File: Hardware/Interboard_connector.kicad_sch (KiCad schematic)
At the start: 2 parts, among them J201 Chainbus in, J202 Chainbus Out

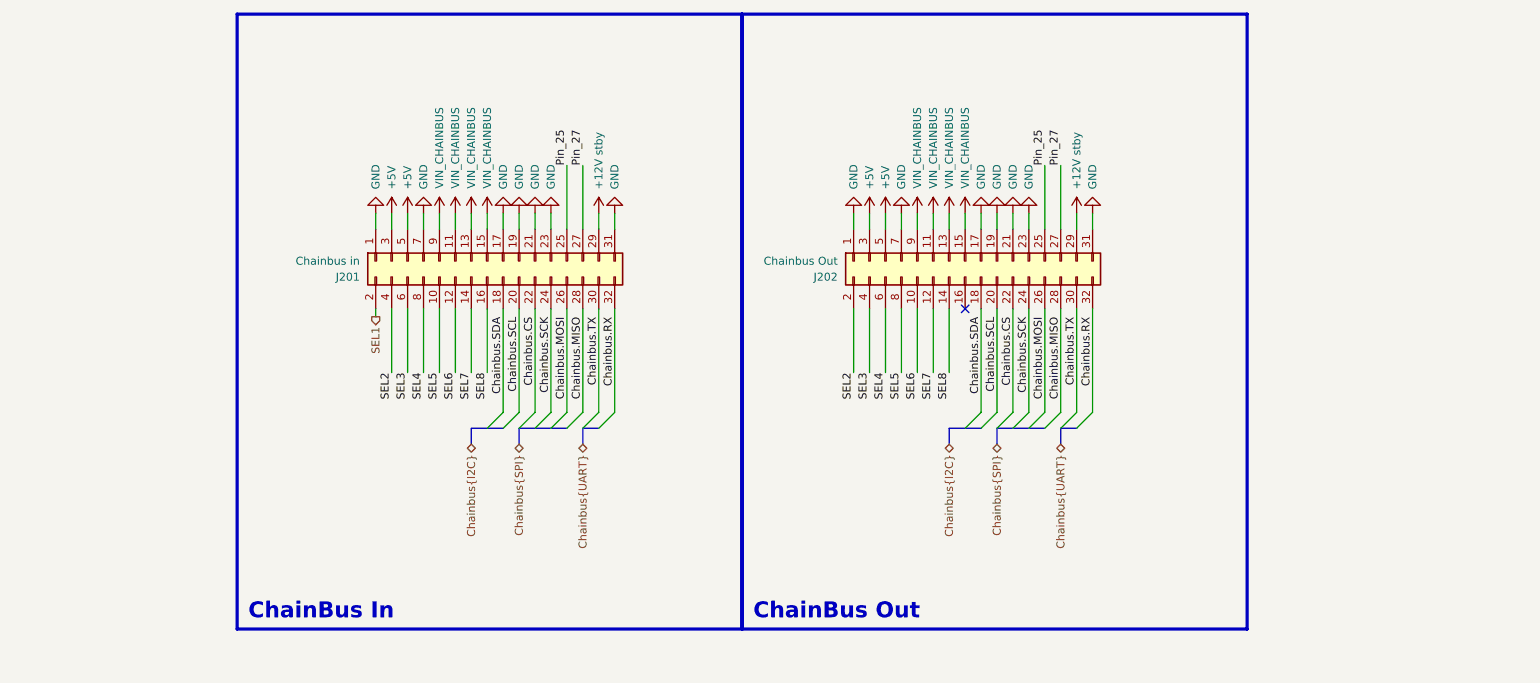
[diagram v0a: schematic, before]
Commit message: updated settings to be same as ModuCard BM3
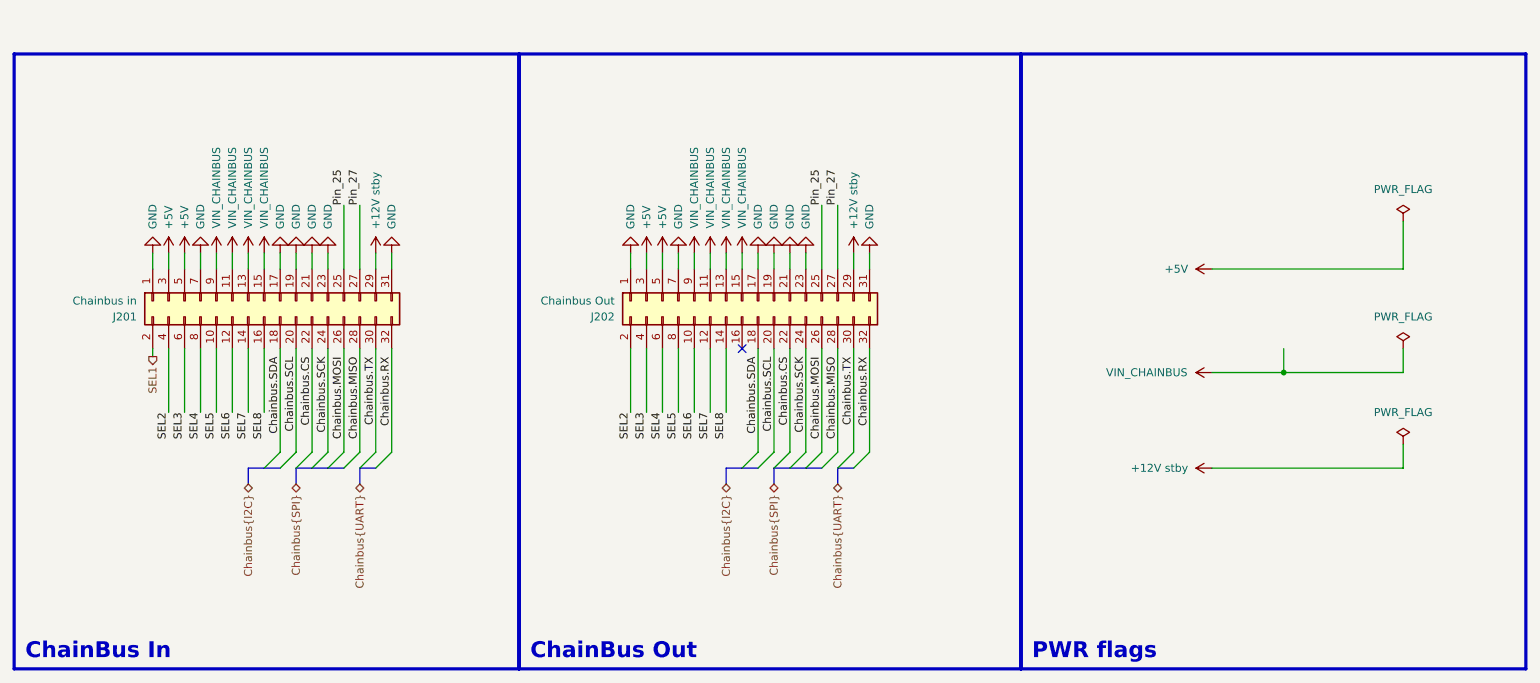
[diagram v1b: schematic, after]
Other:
- note added: "PWR flags"
- moved on the sheet: J201, J202

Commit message: finished PCB
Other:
- title: MMS3 Hat template small (Change Me) -> MMS3_hat_air_quality
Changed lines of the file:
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@@
 	(paper "A4")
 	(title_block
-		(title "MMS3 Hat template small (Change Me)")
-		(date "2077-13-75")
-		(rev "A")
+		(title "MMS3_hat_air_quality")
+		(date "2026-08-07")
+		(rev "1.0")
 		(company "MiniModucard System")
 		(comment 1 "Wojciech Szafrański")
@@
 		)
 		(instances
-			(project "MMS3_hat_templates"
+			(project "MMS3_hat_air_quality"
 				(path "/6596548a-44e0-46d8-8624-fd71cf4a3e17/fdb595ff-e94b-4e80-8fe7-e7d367588ab2"
 					(reference "#PWR0207")
@@
 		)
 		(instances
-			(project "MMS3_hat_templates"
+			(project "MMS3_hat_air_quality"
 				(path "/6596548a-44e0-46d8-8624-fd71cf4a3e17/fdb595ff-e94b-4e80-8fe7-e7d367588ab2"
 					(reference "#PWR0215")
@@
 		)
 		(instances
-			(project "MMS3_hat_templates"
+			(project "MMS3_hat_air_quality"
 				(path "/6596548a-44e0-46d8-8624-fd71cf4a3e17/fdb595ff-e94b-4e80-8fe7-e7d367588ab2"
 					(reference "#PWR0213")
@@
 		)
 		(instances
-			(project "MMS3_hat_templates"
+			(project "MMS3_hat_air_quality"
 				(path "/6596548a-44e0-46d8-8624-fd71cf4a3e17/fdb595ff-e94b-4e80-8fe7-e7d367588ab2"
 					(reference "#PWR0205")
@@
 		)
 		(instances
-			(project "MMS3_hat_templates"
+			(project "MMS3_hat_air_quality"
 				(path "/6596548a-44e0-46d8-8624-fd71cf4a3e17/fdb595ff-e94b-4e80-8fe7-e7d367588ab2"
 					(reference "#PWR0222")
@@
 		)
 		(instances
-			(project "MMS3_hat_templates"
+			(project "MMS3_hat_air_quality"
 				(path "/6596548a-44e0-46d8-8624-fd71cf4a3e17/fdb595ff-e94b-4e80-8fe7-e7d367588ab2"
 					(reference "#PWR0229")
@@
 		)
 		(instances
-			(project "MMS3_hat_templates"
+			(project "MMS3_hat_air_quality"
 				(path "/6596548a-44e0-46d8-8624-fd71cf4a3e17/fdb595ff-e94b-4e80-8fe7-e7d367588ab2"
 					(reference "#PWR0211")
@@
 		)
 		(instances
-			(project "MMS3_hat_templates"
+			(project "MMS3_hat_air_quality"
 				(path "/6596548a-44e0-46d8-8624-fd71cf4a3e17/fdb595ff-e94b-4e80-8fe7-e7d367588ab2"
 					(reference "#PWR0219")
@@
 		)
 		(instances
-			(project "MMS3_hat_templates"
+			(project "MMS3_hat_air_quality"
 				(path "/6596548a-44e0-46d8-8624-fd71cf4a3e17/fdb595ff-e94b-4e80-8fe7-e7d367588ab2"
 					(reference "#PWR0203")
@@
 		)
 		(instances
-			(project "MMS3_hat_templates"
+			(project "MMS3_hat_air_quality"
 				(path "/6596548a-44e0-46d8-8624-fd71cf4a3e17/fdb595ff-e94b-4e80-8fe7-e7d367588ab2"
 					(reference "#PWR0221")
@@
 		)
 		(instances
-			(project "MMS3_hat_templates"
+			(project "MMS3_hat_air_quality"
 				(path "/6596548a-44e0-46d8-8624-fd71cf4a3e17/fdb595ff-e94b-4e80-8fe7-e7d367588ab2"
 					(reference "#FLG0203")
@@
 		)
 		(instances
-			(project "MMS3_hat_templates"
+			(project "MMS3_hat_air_quality"
 				(path "/6596548a-44e0-46d8-8624-fd71cf4a3e17/fdb595ff-e94b-4e80-8fe7-e7d367588ab2"
 					(reference "#PWR0224")
@@
 		)
 		(instances
-			(project "MMS3_hat_templates"
+			(project "MMS3_hat_air_quality"
 				(path "/6596548a-44e0-46d8-8624-fd71cf4a3e17/fdb595ff-e94b-4e80-8fe7-e7d367588ab2"
 					(reference "#PWR0230")
@@
 		)
 		(instances
-			(project "MMS3_hat_templates"
+			(project "MMS3_hat_air_quality"
 				(path "/6596548a-44e0-46d8-8624-fd71cf4a3e17/fdb595ff-e94b-4e80-8fe7-e7d367588ab2"
 					(reference "J202")
@@
 		)
 		(instances
-			(project "MMS3_hat_templates"
+			(project "MMS3_hat_air_quality"
 				(path "/6596548a-44e0-46d8-8624-fd71cf4a3e17/fdb595ff-e94b-4e80-8fe7-e7d367588ab2"
 					(reference "#PWR0226")
@@
 		)
 		(instances
-			(project "MMS3_hat_templates"
+			(project "MMS3_hat_air_quality"
 				(path "/6596548a-44e0-46d8-8624-fd71cf4a3e17/fdb595ff-e94b-4e80-8fe7-e7d367588ab2"
 					(reference "#PWR0231")
@@
 		)
 		(instances
-			(project "MMS3_hat_templates"
+			(project "MMS3_hat_air_quality"
 				(path "/6596548a-44e0-46d8-8624-fd71cf4a3e17/fdb595ff-e94b-4e80-8fe7-e7d367588ab2"
 					(reference "#PWR0208")
@@
 		)
 		(instances
-			(project "MMS3_hat_templates"
+			(project "MMS3_hat_air_quality"
 				(path "/6596548a-44e0-46d8-8624-fd71cf4a3e17/fdb595ff-e94b-4e80-8fe7-e7d367588ab2"
 					(reference "J201")
@@
 		)
 		(instances
-			(project "MMS3_hat_templates"
+			(project "MMS3_hat_air_quality"
 				(path "/6596548a-44e0-46d8-8624-fd71cf4a3e17/fdb595ff-e94b-4e80-8fe7-e7d367588ab2"
 					(reference "#PWR0216")
@@
 		)
 		(instances
-			(project "MMS3_hat_templates"
+			(project "MMS3_hat_air_quality"
 				(path "/6596548a-44e0-46d8-8624-fd71cf4a3e17/fdb595ff-e94b-4e80-8fe7-e7d367588ab2"
 					(reference "#PWR0227")
@@
 		)
 		(instances
-			(project "MMS3_hat_templates"
+			(project "MMS3_hat_air_quality"
 				(path "/6596548a-44e0-46d8-8624-fd71cf4a3e17/fdb595ff-e94b-4e80-8fe7-e7d367588ab2"
 					(reference "#PWR0218")
@@
 		)
 		(instances
-			(project "MMS3_hat_templates"
+			(project "MMS3_hat_air_quality"
 				(path "/6596548a-44e0-46d8-8624-fd71cf4a3e17/fdb595ff-e94b-4e80-8fe7-e7d367588ab2"
 					(reference "#FLG0202")
@@
 		)
 		(instances
-			(project "MMS3_hat_templates"
+			(project "MMS3_hat_air_quality"
 				(path "/6596548a-44e0-46d8-8624-fd71cf4a3e17/fdb595ff-e94b-4e80-8fe7-e7d367588ab2"
 					(reference "#PWR0228")
@@
 		)
 		(instances
-			(project "MMS3_hat_templates"
+			(project "MMS3_hat_air_quality"
 				(path "/6596548a-44e0-46d8-8624-fd71cf4a3e17/fdb595ff-e94b-4e80-8fe7-e7d367588ab2"
 					(reference "#PWR0220")
@@
 		)
 		(instances
-			(project "MMS3_hat_templates"
+			(project "MMS3_hat_air_quality"
 				(path "/6596548a-44e0-46d8-8624-fd71cf4a3e17/fdb595ff-e94b-4e80-8fe7-e7d367588ab2"
 					(reference "#PWR0201")
@@
 		)
 		(instances
-			(project "MMS3_hat_templates"
+			(project "MMS3_hat_air_quality"
 				(path "/6596548a-44e0-46d8-8624-fd71cf4a3e17/fdb595ff-e94b-4e80-8fe7-e7d367588ab2"
 					(reference "#PWR0210")
@@
 		)
 		(instances
-			(project "MMS3_hat_templates"
+			(project "MMS3_hat_air_quality"
 				(path "/6596548a-44e0-46d8-8624-fd71cf4a3e17/fdb595ff-e94b-4e80-8fe7-e7d367588ab2"
 					(reference "#PWR0217")
@@
 		)
 		(instances
-			(project "MMS3_hat_templates"
+			(project "MMS3_hat_air_quality"
 				(path "/6596548a-44e0-46d8-8624-fd71cf4a3e17/fdb595ff-e94b-4e80-8fe7-e7d367588ab2"
 					(reference "#PWR0206")
@@
 		)
 		(instances
-			(project "MMS3_hat_templates"
+			(project "MMS3_hat_air_quality"
 				(path "/6596548a-44e0-46d8-8624-fd71cf4a3e17/fdb595ff-e94b-4e80-8fe7-e7d367588ab2"
 					(reference "#PWR0214")
@@
 		)
 		(instances
-			(project "MMS3_hat_templates"
+			(project "MMS3_hat_air_quality"
 				(path "/6596548a-44e0-46d8-8624-fd71cf4a3e17/fdb595ff-e94b-4e80-8fe7-e7d367588ab2"
 					(reference "#FLG0201")
@@
 		)
 		(instances
-			(project "MMS3_hat_templates"
+			(project "MMS3_hat_air_quality"
 				(path "/6596548a-44e0-46d8-8624-fd71cf4a3e17/fdb595ff-e94b-4e80-8fe7-e7d367588ab2"
 					(reference "#PWR0225")
@@
 		)
 		(instances
-			(project "MMS3_hat_templates"
+			(project "MMS3_hat_air_quality"
 				(path "/6596548a-44e0-46d8-8624-fd71cf4a3e17/fdb595ff-e94b-4e80-8fe7-e7d367588ab2"
 					(reference "#PWR0204")
@@
 		)
 		(instances
-			(project "MMS3_hat_templates"
+			(project "MMS3_hat_air_quality"
 				(path "/6596548a-44e0-46d8-8624-fd71cf4a3e17/fdb595ff-e94b-4e80-8fe7-e7d367588ab2"
 					(reference "#PWR0209")
@@
 		)
 		(instances
-			(project "MMS3_hat_templates"
+			(project "MMS3_hat_air_quality"
 				(path "/6596548a-44e0-46d8-8624-fd71cf4a3e17/fdb595ff-e94b-4e80-8fe7-e7d367588ab2"
 					(reference "#PWR0223")
@@
 		)
 		(instances
-			(project "MMS3_hat_templates"
+			(project "MMS3_hat_air_quality"
 				(path "/6596548a-44e0-46d8-8624-fd71cf4a3e17/fdb595ff-e94b-4e80-8fe7-e7d367588ab2"
 					(reference "#PWR0202")
@@
 		)
 		(instances
-			(project "MMS3_hat_templates"
+			(project "MMS3_hat_air_quality"
 				(path "/6596548a-44e0-46d8-8624-fd71cf4a3e17/fdb595ff-e94b-4e80-8fe7-e7d367588ab2"
 					(reference "#PWR0212")
